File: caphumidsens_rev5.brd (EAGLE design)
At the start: 110 x 10 mm, 13 parts, among them IC1 ATtiny25/45/85/13A

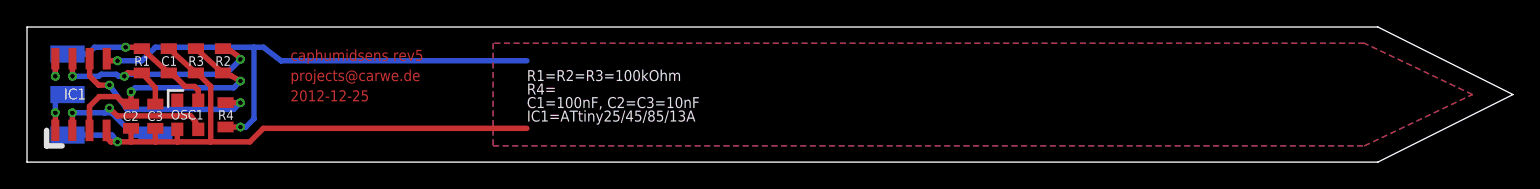
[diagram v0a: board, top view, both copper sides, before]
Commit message: reworked silkscreen
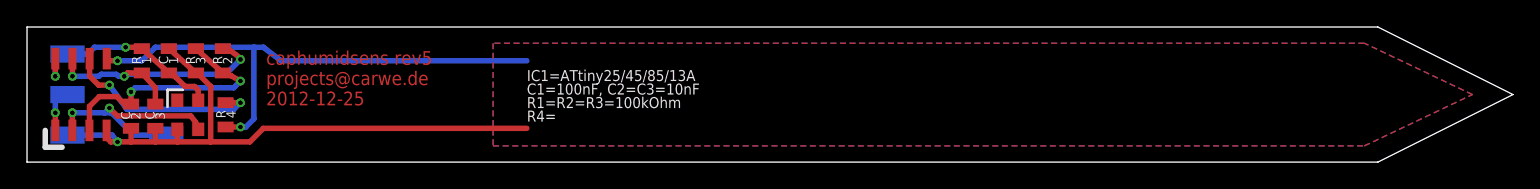
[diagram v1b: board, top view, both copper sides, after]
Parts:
- moved (OUT2) 0.80 mm to (10.3, 2.00)
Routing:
- net CLOCK_IN: track 16.0 -> 16.8 mm
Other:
- board text added: "1"
- board text added: "2"
- board text added: "3"
- board text added: "4"
- board text added: "C"
- board text added: "R"
- board text removed: "OSC1"
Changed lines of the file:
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@@
 <wire x1="100" y1="10" x2="0" y2="10" width="0" layer="20"/>
 <wire x1="0" y1="10" x2="0" y2="0" width="0" layer="20"/>
-<wire x1="1.45" y1="1.2" x2="2.6" y2="1.2" width="0.4064" layer="25"/>
-<text x="19.5" y="7.5" size="0.8128" layer="1" font="vector" ratio="15">caphumidsens rev5</text>
-<text x="19.5" y="6" size="0.8128" layer="1" font="vector" ratio="15">projects@carwe.de</text>
-<text x="37" y="6" size="0.8128" layer="25" font="vector" ratio="15">R1=R2=R3=100kOhm</text>
-<text x="37" y="5" size="0.8128" layer="25" font="vector" ratio="15">R4=</text>
-<text x="37" y="4" size="0.8128" layer="25" font="vector" ratio="15">C1=100nF, C2=C3=10nF</text>
-<text x="37" y="3" size="0.8128" layer="25" font="vector" ratio="15">IC1=ATtiny25/45/85/13A</text>
-<wire x1="10.45" y1="4.1" x2="10.45" y2="5.3" width="0.2" layer="25"/>
-<wire x1="1.45" y1="1.2" x2="1.45" y2="2.35" width="0.4064" layer="25"/>
-<text x="19.5" y="6" size="0.8128" layer="29" font="vector" ratio="15">projects@carwe.de</text>
-<text x="19.5" y="7.5" size="0.8128" layer="29" font="vector" ratio="15">caphumidsens rev5</text>
-<wire x1="11.55" y1="5.3" x2="10.45" y2="5.3" width="0.2" layer="25"/>
-<text x="10.65" y="3.15" size="0.7112" layer="25" font="vector" ratio="15">OSC1</text>
-<text x="19.5" y="4.5" size="0.8128" layer="1" font="vector" ratio="15">2012-12-25</text>
-<text x="19.5" y="4.5" size="0.8128" layer="29" font="vector" ratio="15">2012-12-25</text>
+<wire x1="1.35" y1="1.1" x2="2.6" y2="1.1" width="0.4064" layer="25"/>
+<text x="17.7" y="7.2" size="1.016" layer="1" font="vector" ratio="15">caphumidsens rev5</text>
+<text x="17.7" y="5.7" size="1.016" layer="1" font="vector" ratio="15">projects@carwe.de</text>
+<text x="37" y="4" size="0.8128" layer="25" font="vector" ratio="15">R1=R2=R3=100kOhm</text>
+<text x="37" y="3" size="0.8128" layer="25" font="vector" ratio="15">R4=</text>
+<text x="37" y="5" size="0.8128" layer="25" font="vector" ratio="15">C1=100nF, C2=C3=10nF</text>
+<text x="37" y="6" size="0.8128" layer="25" font="vector" ratio="15">IC1=ATtiny25/45/85/13A</text>
+<wire x1="10.4" y1="4.1" x2="10.4" y2="5.35" width="0.2" layer="25"/>
+<wire x1="1.35" y1="1.1" x2="1.35" y2="2.35" width="0.4064" layer="25"/>
+<text x="17.7" y="5.7" size="1.016" layer="29" font="vector" ratio="15">projects@carwe.de</text>
+<text x="17.7" y="7.2" size="1.016" layer="29" font="vector" ratio="15">caphumidsens rev5</text>
+<wire x1="11.55" y1="5.35" x2="10.4" y2="5.35" width="0.2" layer="25"/>
+<text x="17.7" y="4.2" size="1.016" layer="1" font="vector" ratio="15">2012-12-25</text>
+<text x="17.7" y="4.2" size="1.016" layer="29" font="vector" ratio="15">2012-12-25</text>
+<text x="15.45" y="3.25" size="0.7" layer="21" font="vector" ratio="15" distance="5" rot="R90">4</text>
+<text x="10.2" y="3.15" size="0.7" layer="21" font="vector" ratio="15" distance="5" rot="R90">3</text>
+<text x="8.4" y="3.15" size="0.7" layer="21" font="vector" ratio="15" distance="5" rot="R90">2</text>
+<text x="9.2" y="7.25" size="0.7" layer="21" font="vector" ratio="15" distance="5" rot="R90">1</text>
+<text x="11.2" y="7.25" size="0.7" layer="21" font="vector" ratio="15" distance="5" rot="R90">1</text>
+<text x="13.2" y="7.25" size="0.7" layer="21" font="vector" ratio="15" distance="5" rot="R90">3</text>
+<text x="15.2" y="7.25" size="0.7" layer="21" font="vector" ratio="15" distance="5" rot="R90">2</text>
+<text x="14.45" y="7.25" size="0.7" layer="21" font="vector" ratio="15" distance="5" rot="R90">R</text>
+<text x="12.45" y="7.25" size="0.7" layer="21" font="vector" ratio="15" distance="5" rot="R90">R</text>
+<text x="10.45" y="7.25" size="0.7" layer="21" font="vector" ratio="15" distance="5" rot="R90">C</text>
+<text x="8.45" y="7.25" size="0.7" layer="21" font="vector" ratio="15" distance="5" rot="R90">R</text>
+<text x="7.65" y="3.15" size="0.7" layer="21" font="vector" ratio="15" distance="5" rot="R90">C</text>
+<text x="9.45" y="3.15" size="0.7" layer="21" font="vector" ratio="15" distance="5" rot="R90">C</text>
+<text x="14.7" y="3.25" size="0.7" layer="21" font="vector" ratio="15" distance="5" rot="R90">R</text>
 </plain>
 <attributes>
@@
 </class>
 </classes>
-<designrules name="OSHpark">
+<designrules name="LaenPCBOrder">
 <description language="de">&lt;b&gt;EAGLE Design Rules&lt;/b&gt;
 &lt;p&gt;
@@
 <attribute name="MF" value="" x="21.78" y="1.19" size="1.778" layer="27" display="off"/>
 <attribute name="OC_FARNELL" value="1455135" x="21.78" y="1.19" size="1.778" layer="27" display="off"/>
-<attribute name="NAME" x="4.359" y="5.4425" size="0.8128" layer="25" font="vector" ratio="15" rot="R180"/>
 <attribute name="VALUE" x="4.564" y="1.341" size="0.8128" layer="27" ratio="10" rot="R90"/>
 </element>
 <element name="R2" library="SparkFun" package="0805" value="100k" x="14.5" y="7.5" smashed="yes" rot="R270">
-<attribute name="NAME" x="13.938" y="7.1255" size="0.7112" layer="25" font="vector" ratio="15"/>
 <attribute name="VALUE" x="14.897" y="6.484" size="0.8128" layer="27" rot="R90"/>
 </element>
 <element name="R3" library="SparkFun" package="0805" value="100k" x="12.5" y="7.5" smashed="yes" rot="R90">
-<attribute name="NAME" x="11.938" y="7.1255" size="0.7112" layer="25" font="vector" ratio="15"/>
 <attribute name="VALUE" x="12.103" y="8.516" size="0.8128" layer="27" rot="R270"/>
 </element>
 <element name="R1" library="SparkFun" package="0805" value="100k" x="8.5" y="7.5" smashed="yes" rot="R270">
-<attribute name="NAME" x="7.938" y="7.1255" size="0.7112" layer="25" font="vector" ratio="15"/>
 <attribute name="VALUE" x="8.103" y="8.516" size="0.8128" layer="27" rot="R270"/>
 </element>
 <element name="C1" library="SparkFun" package="0805" value="100n" x="10.5" y="7.5" smashed="yes" rot="R270">
-<attribute name="NAME" x="9.938" y="7.1255" size="0.7112" layer="25" font="vector" ratio="15"/>
 <attribute name="VALUE" x="10.897" y="6.484" size="0.8128" layer="27" rot="R90"/>
 </element>
 <element name="OSC1" library="seb" package="XO32" value="to be defined" x="11.9" y="3.5" rot="R90"/>
 <element name="R4" library="SparkFun" package="0805" value="to be defined" x="14.7" y="3.5" smashed="yes" rot="R90">
-<attribute name="NAME" x="14.138" y="3.1255" size="0.7112" layer="25" font="vector" ratio="15"/>
 <attribute name="VALUE" x="15.097" y="2.484" size="0.8128" layer="27" rot="R90"/>
 </element>
 <element name="C3" library="SparkFun" package="0805" value="10n" x="9.5" y="3.4" smashed="yes" rot="R90">
-<attribute name="NAME" x="8.9" y="3.05" size="0.7112" layer="25" font="vector" ratio="15"/>
 <attribute name="VALUE" x="9.103" y="4.116" size="0.8128" layer="27" rot="R270"/>
 </element>
 <element name="C2" library="SparkFun" package="0805" value="10n" x="7.7" y="3.4" smashed="yes" rot="R270">
-<attribute name="NAME" x="7.1" y="3.05" size="0.7112" layer="25" font="vector" ratio="15"/>
 <attribute name="VALUE" x="7.303" y="3.916" size="0.8128" layer="27" rot="R270"/>
 </element>
-<element name="(OUT2)" library="wirepad" package="SMD1,27-2,54" value="WIREPADSMD2,54-5,08" x="9.5" y="2" smashed="yes" rot="MR90">
-<attribute name="VALUE" x="9.5" y="2" size="0.0254" layer="28" rot="MR90"/>
-<attribute name="NAME" x="14.8" y="1.6" size="0.8128" layer="26" font="vector" ratio="15" rot="MR0"/>
+<element name="(OUT2)" library="wirepad" package="SMD1,27-2,54" value="WIREPADSMD2,54-5,08" x="10.3" y="2" smashed="yes" rot="MR90">
+<attribute name="VALUE" x="10.3" y="2" size="0.0254" layer="28" rot="MR90"/>
+<attribute name="NAME" x="13" y="5.1" size="0.8128" layer="26" font="vector" ratio="15" rot="SMR270"/>
 </element>
 </elements>
@@
 <wire x1="5.75" y1="3.65" x2="6.25" y2="3.65" width="0.4064" layer="16"/>
 <wire x1="6.25" y1="3.65" x2="7.9" y2="2" width="0.4064" layer="16"/>
-<wire x1="7.9" y1="2" x2="9.5" y2="2" width="0.4064" layer="16"/>
+<wire x1="7.9" y1="2" x2="10.3" y2="2" width="0.4064" layer="16"/>
 </signal>
 <signal name="OUTPUT_OR_DEBUGWIRE">
